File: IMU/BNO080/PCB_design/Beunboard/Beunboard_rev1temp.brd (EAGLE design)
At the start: 76.2 x 78.4 mm, 15 parts, among them U1 XMEGABOARD-REV1.00-20150419DIP, U2 SPARKFUN_BNO080SPARKFUN_BNO080, U3 NAVSPARK_MININAVSPARK_MINI

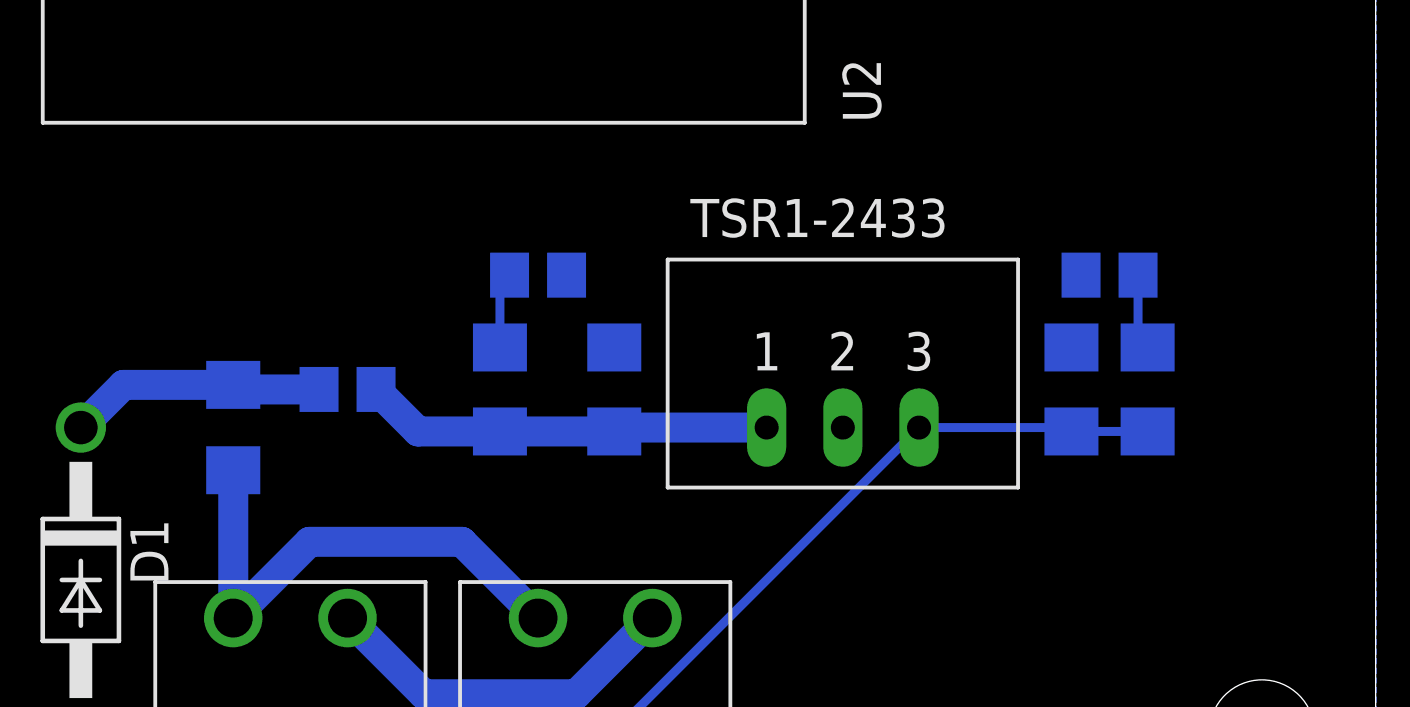
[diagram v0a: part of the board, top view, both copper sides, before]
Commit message: AVR SPI exmpl, board designs
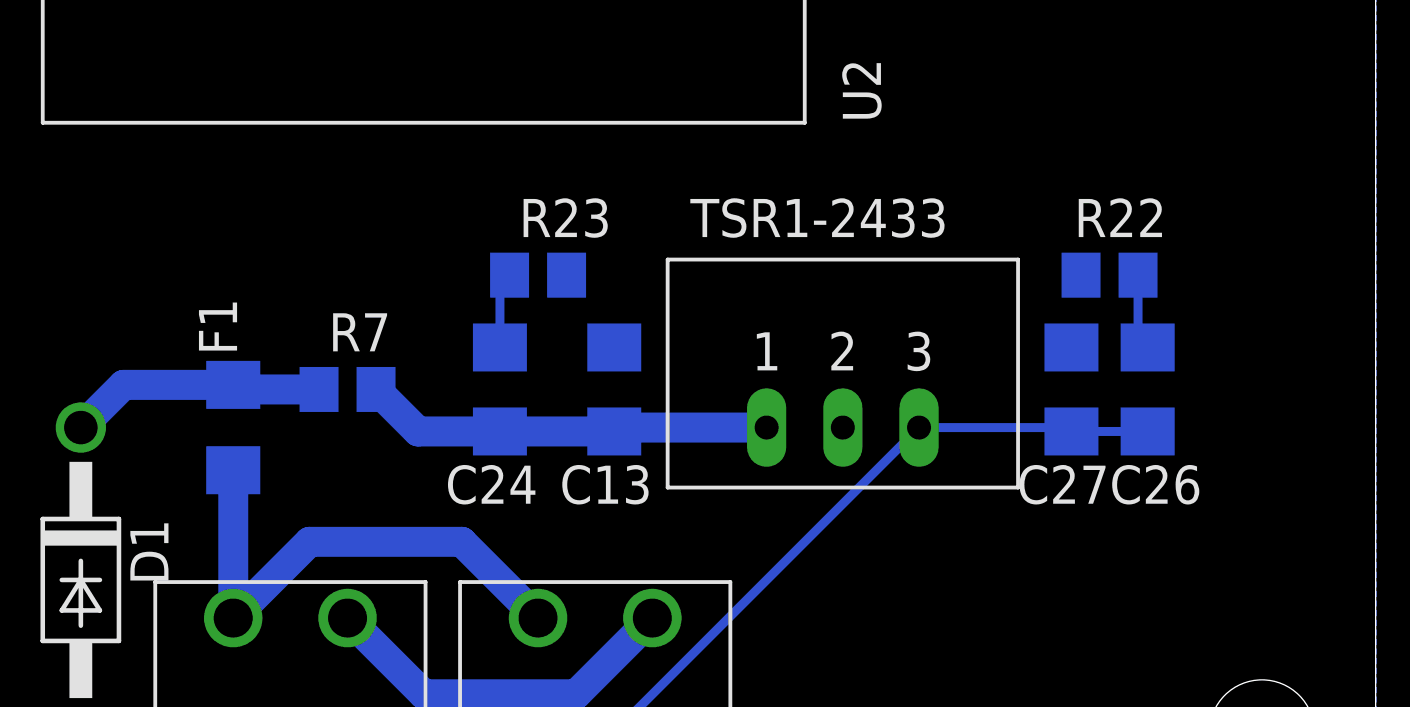
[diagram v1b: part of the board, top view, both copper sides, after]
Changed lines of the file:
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@@
 <elements>
 <element name="C13" library="rcl" library_urn="urn:adsk.eagle:library:334" package="C1206" package3d_urn="urn:adsk.eagle:package:23618/2" value="10uF" x="50.8" y="15.24" smashed="yes" rot="MR90">
-<attribute name="NAME" x="52.07" y="13.97" size="1.27" layer="26" rot="MR90"/>
+<attribute name="NAME" x="52.07" y="12.7" size="1.27" layer="25" rot="R180"/>
 <attribute name="SPICEPREFIX" value="C" x="-54.61" y="57.15" size="1.778" layer="28" rot="MR90" display="off"/>
-<attribute name="VALUE" x="48.26" y="13.97" size="1.27" layer="28" rot="MR90"/>
+<attribute name="VALUE" x="48.26" y="16.51" size="1.27" layer="27" rot="R270"/>
 </element>
 <element name="C24" library="rcl" library_urn="urn:adsk.eagle:library:334" package="C1206" package3d_urn="urn:adsk.eagle:package:23618/2" value="22uF" x="46.99" y="15.24" smashed="yes" rot="MR90">
-<attribute name="NAME" x="48.26" y="13.97" size="1.27" layer="26" rot="MR90"/>
+<attribute name="NAME" x="48.26" y="12.7" size="1.27" layer="25" rot="R180"/>
 <attribute name="SPICEPREFIX" value="C" x="-58.42" y="63.5" size="1.778" layer="28" rot="MR90" display="off"/>
-<attribute name="VALUE" x="44.45" y="13.97" size="1.27" layer="28" rot="MR90"/>
+<attribute name="VALUE" x="45.72" y="12.7" size="1.27" layer="27" rot="R90"/>
 </element>
 <element name="C26" library="rcl" library_urn="urn:adsk.eagle:library:334" package="C1206" package3d_urn="urn:adsk.eagle:package:23618/2" value="22uF" x="68.58" y="15.24" smashed="yes" rot="MR90">
-<attribute name="NAME" x="69.85" y="13.97" size="1.27" layer="26" rot="MR90"/>
+<attribute name="NAME" x="67.31" y="11.43" size="1.27" layer="25"/>
 <attribute name="SPICEPREFIX" value="C" x="-36.83" y="69.85" size="1.778" layer="28" rot="MR90" display="off"/>
-<attribute name="VALUE" x="66.04" y="13.97" size="1.27" layer="28" rot="MR90"/>
+<attribute name="VALUE" x="71.12" y="13.97" size="1.27" layer="27" rot="R90"/>
 </element>
 <element name="C27" library="rcl" library_urn="urn:adsk.eagle:library:334" package="C1206" package3d_urn="urn:adsk.eagle:package:23618/2" value="10uF" x="66.04" y="15.24" smashed="yes" rot="MR90">
-<attribute name="NAME" x="67.31" y="13.97" size="1.27" layer="26" rot="MR90"/>
+<attribute name="NAME" x="67.31" y="12.7" size="1.27" layer="25" rot="R180"/>
 <attribute name="SPICEPREFIX" value="C" x="-39.37" y="76.2" size="1.778" layer="28" rot="MR90" display="off"/>
-<attribute name="VALUE" x="63.5" y="13.97" size="1.27" layer="28" rot="MR90"/>
+<attribute name="VALUE" x="63.5" y="16.51" size="1.27" layer="27" rot="R270"/>
 </element>
 <element name="D1" library="diode" library_urn="urn:adsk.eagle:library:210" package="DO41-10" package3d_urn="urn:adsk.eagle:package:43336/1" value="1N4004" x="33.02" y="8.89" smashed="yes" rot="R270">
@@
 </element>
 <element name="F1" library="adafruit" package="R1206" value="350mA" x="38.1" y="13.97" smashed="yes" rot="MR90">
-<attribute name="NAME" x="39.243" y="12.573" size="1.27" layer="26" rot="MR90"/>
-<attribute name="VALUE" x="35.687" y="12.573" size="1.27" layer="28" rot="MR90"/>
+<attribute name="NAME" x="38.227" y="16.383" size="1.27" layer="25" rot="R90"/>
+<attribute name="VALUE" x="36.703" y="11.303" size="1.27" layer="27" rot="R90"/>
 </element>
 <element name="POWER1" library="Phoenix-con" package="CON_3.81MM2_SIDE" value="CON_3.81MM2_SIDE" x="48.26" y="7.62" smashed="yes"/>
 <element name="POWER2" library="Phoenix-con" package="CON_3.81MM2_SIDE" value="CON_3.81MM2_SIDE" x="38.1" y="7.62" smashed="yes"/>
 <element name="R22" library="rcl" library_urn="urn:adsk.eagle:library:334" package="R0805" package3d_urn="urn:adsk.eagle:package:23553/2" value="1 Ohm" x="67.31" y="19.05" smashed="yes" rot="MR0">
-<attribute name="NAME" x="67.945" y="20.32" size="1.27" layer="26" rot="MR0"/>
+<attribute name="NAME" x="69.215" y="21.59" size="1.27" layer="25" rot="R180"/>
 <attribute name="SPICEPREFIX" value="R" x="39.37" y="-86.36" size="1.778" layer="28" rot="MR0" display="off"/>
-<attribute name="VALUE" x="67.945" y="16.51" size="1.27" layer="28" rot="MR0"/>
+<attribute name="VALUE" x="69.215" y="19.05" size="1.27" layer="27"/>
 </element>
 <element name="R23" library="rcl" library_urn="urn:adsk.eagle:library:334" package="R0805" package3d_urn="urn:adsk.eagle:package:23553/2" value="1 Ohm" x="48.26" y="19.05" smashed="yes" rot="MR0">
-<attribute name="NAME" x="48.895" y="20.32" size="1.27" layer="26" rot="MR0"/>
+<attribute name="NAME" x="47.625" y="20.32" size="1.27" layer="25"/>
 <attribute name="SPICEPREFIX" value="R" x="12.7" y="-86.36" size="1.778" layer="28" rot="MR0" display="off"/>
-<attribute name="VALUE" x="48.895" y="16.51" size="1.27" layer="28" rot="MR0"/>
+<attribute name="VALUE" x="46.355" y="21.59" size="1.27" layer="27"/>
 </element>
 <element name="R7" library="rcl" library_urn="urn:adsk.eagle:library:334" package="R0805" package3d_urn="urn:adsk.eagle:package:23553/2" value="0.2 Ohm" x="41.91" y="15.24" smashed="yes" rot="MR0">
-<attribute name="NAME" x="42.545" y="16.51" size="1.27" layer="26" rot="MR0"/>
+<attribute name="NAME" x="41.275" y="16.51" size="1.27" layer="25"/>
 <attribute name="SPICEPREFIX" value="R" x="21.59" y="-90.17" size="1.778" layer="28" rot="MR0" display="off"/>
-<attribute name="VALUE" x="42.545" y="12.7" size="1.27" layer="28" rot="MR0"/>
+<attribute name="VALUE" x="38.735" y="17.78" size="1.27" layer="27"/>
 </element>
 <element name="TSR1-2433" library="tracopower" package="TSR1-2433" value="" x="58.42" y="13.97" smashed="yes">
